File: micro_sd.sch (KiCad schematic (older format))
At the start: 1 part, among them U4 MICRO-SD-CONN

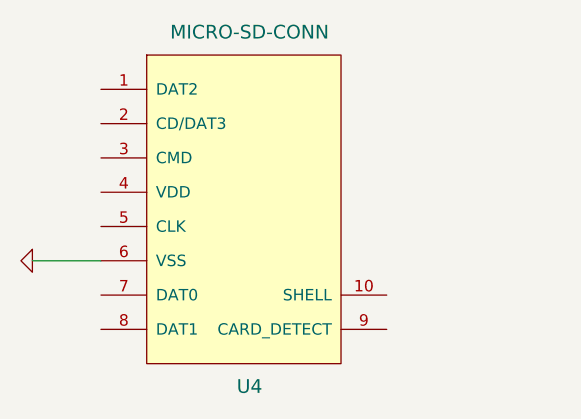
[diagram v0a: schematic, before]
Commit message: Add gps
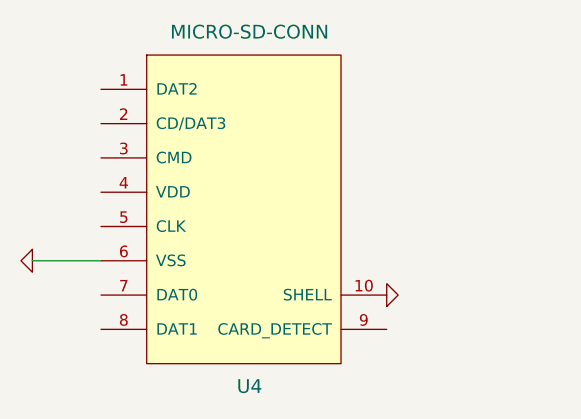
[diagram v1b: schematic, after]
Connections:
- net GND: now also U4.10 (SHELL)
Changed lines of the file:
@@
 $Descr A4 11693 8268
 encoding utf-8
-Sheet 4 10
+Sheet 4 11
 Title ""
 Date ""
@@
 $EndComp
 $Comp
-L GND #PWR7
+L GND #PWR11
 U 1 1 544628AE
 P 3900 3800
-F 0 "#PWR7" H 3900 3800 30  0001 C CNN
+F 0 "#PWR11" H 3900 3800 30  0001 C CNN
 F 1 "GND" H 3900 3730 30  0001 C CNN
 F 2 "" H 3900 3800 60  0000 C CNN
@@
 Wire Wire Line
 	3900 3800 4200 3800
+$Comp
+L GND #PWR12
+U 1 1 546153A2
+P 5450 3950
+F 0 "#PWR12" H 5450 3950 30  0001 C CNN
+F 1 "GND" H 5450 3880 30  0001 C CNN
+F 2 "" H 5450 3950 60  0000 C CNN
+F 3 "" H 5450 3950 60  0000 C CNN
+	1    5450 3950
+	0    -1   -1   0
+$EndComp
 $EndSCHEMATC

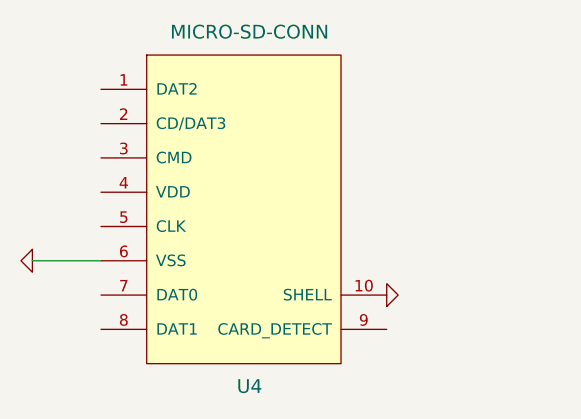
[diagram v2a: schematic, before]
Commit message: More connections
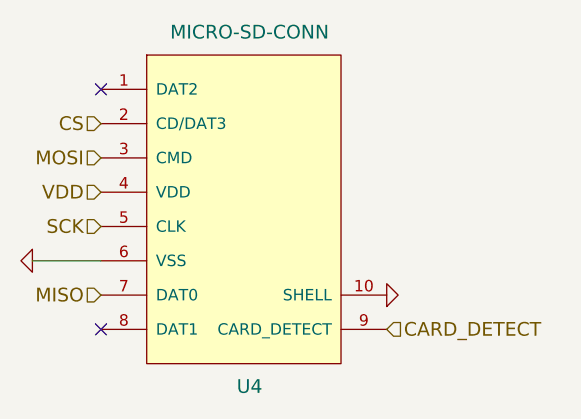
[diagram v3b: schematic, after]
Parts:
- U4: footprint (none) -> buq2:MICRO-SD-CONN-AMPHENOL-PUSH-PUSH
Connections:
- net CS: now reaches U4.2 (CD/DAT3)
- net MOSI: now reaches U4.3 (CMD)
- net VDD: now reaches U4.4 (VDD)
- net SCK: now reaches U4.5 (CLK)
- net MISO: now reaches U4.7 (DAT0)
- net CARD_DETECT: now reaches U4.9 (CARD_DETECT)
- no-connect marks 0 -> 2
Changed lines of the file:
@@
 F 0 "U4" H 4850 3050 60  0000 C CNN
 F 1 "MICRO-SD-CONN" H 4850 4600 60  0000 C CNN
-F 2 "" H 4850 3700 60  0001 C CNN
+F 2 "buq2:MICRO-SD-CONN-AMPHENOL-PUSH-PUSH" H 4850 3700 60  0001 C CNN
 F 3 "" H 4850 3700 60  0000 C CNN
 	1    4850 3700
@@
 $EndComp
 $Comp
-L GND #PWR11
+L GND #PWR011
 U 1 1 544628AE
 P 3900 3800
-F 0 "#PWR11" H 3900 3800 30  0001 C CNN
+F 0 "#PWR011" H 3900 3800 30  0001 C CNN
 F 1 "GND" H 3900 3730 30  0001 C CNN
 F 2 "" H 3900 3800 60  0000 C CNN
@@
 	3900 3800 4200 3800
 $Comp
-L GND #PWR12
+L GND #PWR012
 U 1 1 546153A2
 P 5450 3950
-F 0 "#PWR12" H 5450 3950 30  0001 C CNN
+F 0 "#PWR012" H 5450 3950 30  0001 C CNN
 F 1 "GND" H 5450 3880 30  0001 C CNN
 F 2 "" H 5450 3950 60  0000 C CNN
@@
 	0    -1   -1   0
 $EndComp
+Text HLabel 4200 3500 0    60   Input ~ 0
+VDD
+Text HLabel 4200 3650 0    60   Input ~ 0
+SCK
+Text HLabel 4200 3950 0    60   Input ~ 0
+MISO
+Text HLabel 4200 3350 0    60   Input ~ 0
+MOSI
+Text HLabel 4200 3200 0    60   Input ~ 0
+CS
+NoConn ~ 4200 3050
+NoConn ~ 4200 4100
+Text HLabel 5450 4100 2    60   Input ~ 0
+CARD_DETECT
 $EndSCHEMATC

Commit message: Add flash and ram. Some connections and DRC cleaning
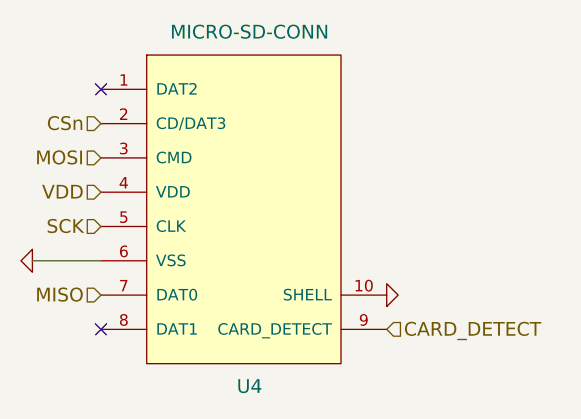
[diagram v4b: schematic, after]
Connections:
- net CS renamed CSn
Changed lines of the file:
@@
 $Descr A4 11693 8268
 encoding utf-8
-Sheet 4 12
+Sheet 4 13
 Title ""
 Date ""
@@
 $EndComp
 $Comp
-L GND #PWR011
+L GND #PWR012
 U 1 1 544628AE
 P 3900 3800
-F 0 "#PWR011" H 3900 3800 30  0001 C CNN
+F 0 "#PWR012" H 3900 3800 30  0001 C CNN
 F 1 "GND" H 3900 3730 30  0001 C CNN
 F 2 "" H 3900 3800 60  0000 C CNN
@@
 	3900 3800 4200 3800
 $Comp
-L GND #PWR012
+L GND #PWR013
 U 1 1 546153A2
 P 5450 3950
-F 0 "#PWR012" H 5450 3950 30  0001 C CNN
+F 0 "#PWR013" H 5450 3950 30  0001 C CNN
 F 1 "GND" H 5450 3880 30  0001 C CNN
 F 2 "" H 5450 3950 60  0000 C CNN
@@
 MOSI
 Text HLabel 4200 3200 0    60   Input ~ 0
-CS
+CSn
 NoConn ~ 4200 3050
 NoConn ~ 4200 4100
